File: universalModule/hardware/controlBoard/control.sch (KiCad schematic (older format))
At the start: 47 parts, among them J1 ESP_JTAG, J2 OLED_DISPLAY, Q4 BC817, Q5 BC817, SW3 SW_Push, SW4 SW_Push, SW5 SW_Push, SW6 SW_Push, SW7 SW_Push, U6 ESP32-WROVER, U7 ICM-20948, U8 CP2102N-A01-GQFN28

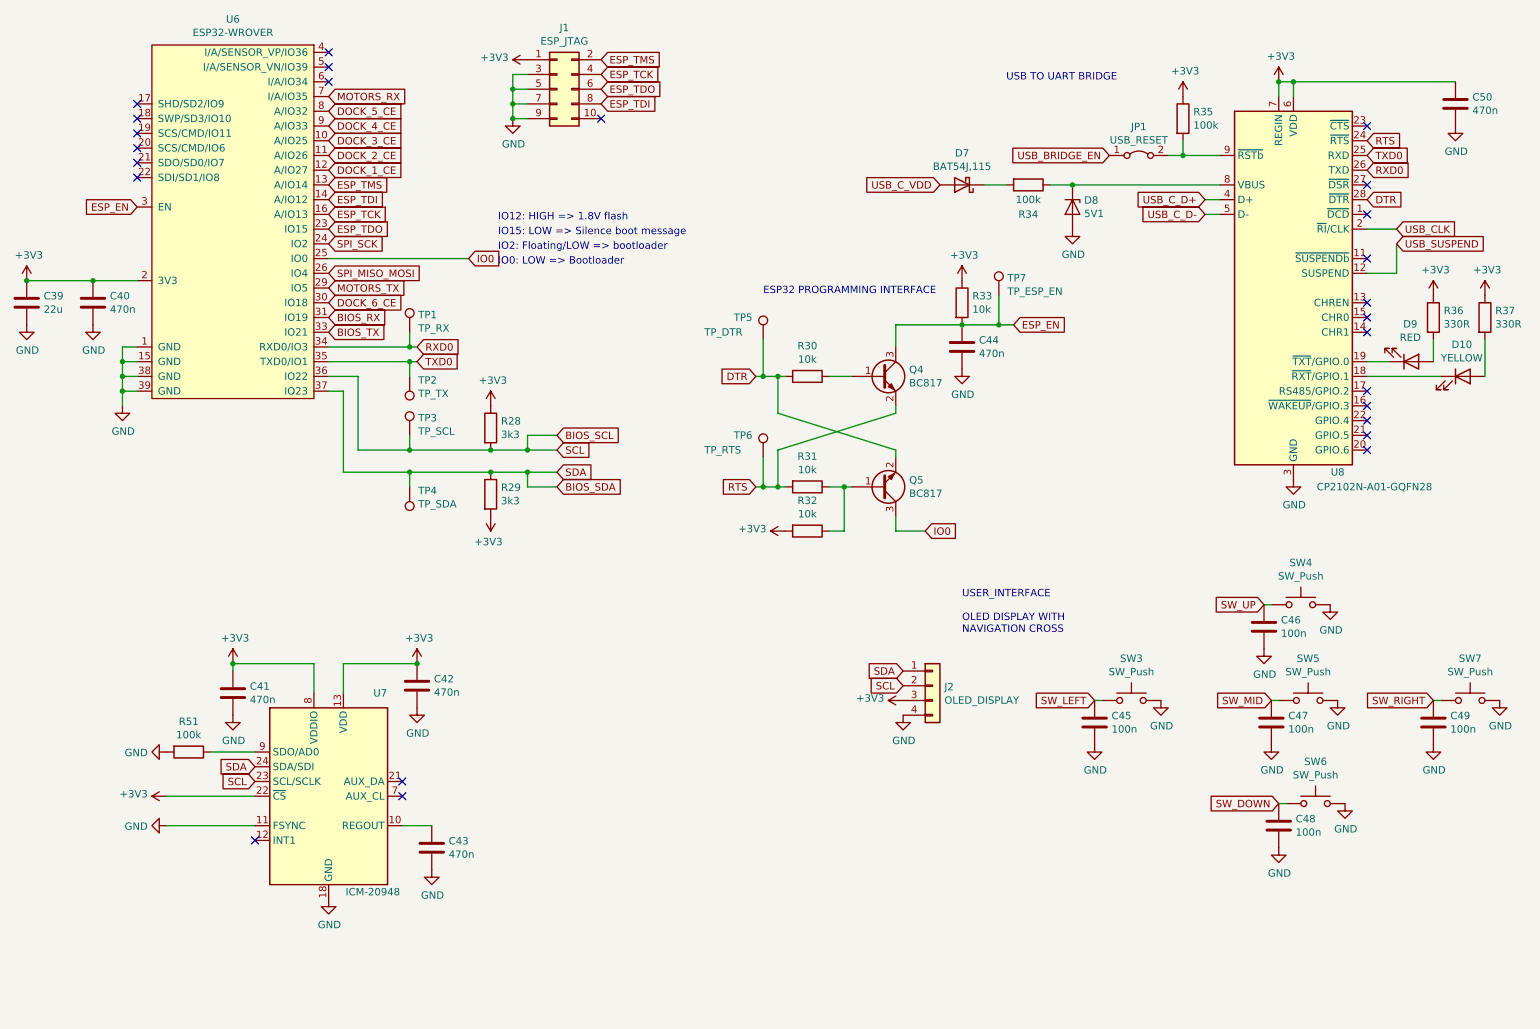
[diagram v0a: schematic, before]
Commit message: universalModule: Route the control boards
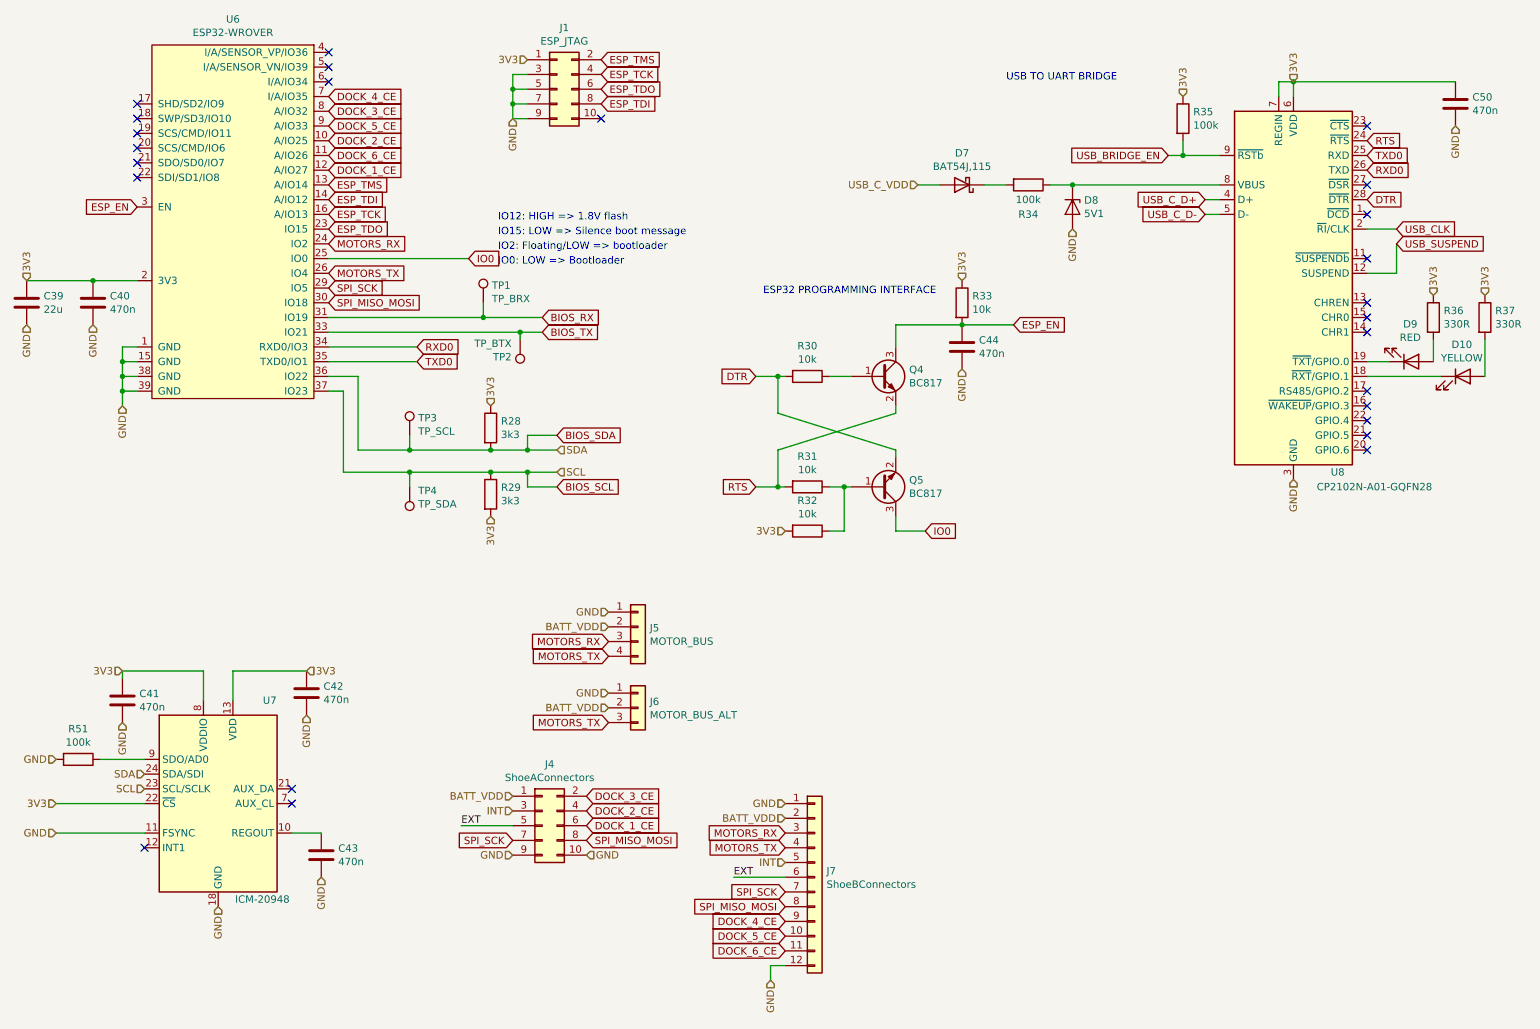
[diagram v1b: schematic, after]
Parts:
- removed C45, C46, C47, C48, C49: 100n, Capacitor_SMD:C_0402_1005Metric, symbol Device:C
- removed J2: OLED_DISPLAY, Connector_PinHeader_2.54mm:PinHeader_1x04_P2.54mm_Vertical, symbol Connector_Generic:Conn_01x04
- removed JP1: USB_RESET, Connector_PinHeader_2.00mm:PinHeader_1x01_P2.00mm_Vertical, symbol Jumper:Jumper_2_Bridged
- removed SW3, SW4, SW5, SW6, SW7: SW_Push, rofi:BUTTON_SMT_G_4_3, symbol Switch:SW_Push
- removed TP5: TP_DTR, TestPoint:TestPoint_Pad_D2.0mm, symbol Connector:TestPoint
- removed TP6: TP_RTS, TestPoint:TestPoint_Pad_D2.0mm, symbol Connector:TestPoint
- removed TP7: TP_ESP_EN, TestPoint:TestPoint_Pad_D2.0mm, symbol Connector:TestPoint
- added J4: ShoeAConnectors, Connector_PinHeader_2.00mm:PinHeader_2x05_P2.00mm_Vertical, symbol Connector_Generic:Conn_02x05_Odd_Even
- added J5: MOTOR_BUS, Connector_PinHeader_2.00mm:PinHeader_1x04_P2.00mm_Vertical, symbol Connector_Generic:Conn_01x04
- added J6: MOTOR_BUS_ALT, Connector_PinHeader_2.00mm:PinHeader_1x03_P2.00mm_Vertical, symbol Connector_Generic:Conn_01x03
- added J7: ShoeBConnectors, rofi:slipRingBrush, symbol Connector_Generic:Conn_01x12
- TP1: value TP_RX -> TP_BRX
- TP2: value TP_TX -> TP_BTX
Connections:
- net BIOS_RX: now also TP1.1
- net BIOS_SCL: now also R29.1, TP4.1, U6.37 (IO23); no longer R28.2, TP3.1, U6.36 (IO22)
- net BIOS_SDA: now also R28.2, TP3.1, U6.36 (IO22); no longer R29.1, TP4.1, U6.37 (IO23)
- net BIOS_TX: now also TP2.1
- net DOCK_1_CE: now also J4.6 (Pin_6)
- net DOCK_2_CE: now also U6.10 (A/IO25), J4.4 (Pin_4); no longer U6.11 (A/IO26)
- net DOCK_3_CE: now also U6.8 (A/IO32), J4.2 (Pin_2); no longer U6.10 (A/IO25)
- net DOCK_4_CE: now also U6.7 (I/A/IO35), J7.9 (Pin_9); no longer U6.9 (A/IO33)
- net DOCK_5_CE: now also U6.9 (A/IO33), J7.10 (Pin_10); no longer U6.8 (A/IO32)
- net DOCK_6_CE: now also U6.11 (A/IO26), J7.11 (Pin_11); no longer U6.30 (IO18)
- net GND: now also J4.10 (Pin_10), J4.9 (Pin_9), J5.1 (Pin_1), J6.1 (Pin_1), J7.1 (Pin_1), J7.12 (Pin_12)
- net MOTORS_RX: now also U6.24 (IO2), J5.3 (Pin_3), J7.3 (Pin_3); no longer U6.7 (I/A/IO35)
- net MOTORS_TX: now also U6.26 (IO4), J5.4 (Pin_4), J6.3 (Pin_3), J7.4 (Pin_4); no longer U6.29 (IO5)
- net RXD0: no longer TP1.1
- net SPI_MISO_MOSI: now also U6.30 (IO18), J4.8 (Pin_8), J7.8 (Pin_8); no longer U6.26 (IO4)
- net SPI_SCK: now also U6.29 (IO5), J4.7 (Pin_7), J7.7 (Pin_7); no longer U6.24 (IO2)
- net TXD0: no longer TP2.1
- net USB_BRIDGE_EN: now also R35.2, U8.9 (~RSTb)
- net +3V3 renamed 3V3
- new net BATT_VDD: J4.1 (Pin_1), J5.2 (Pin_2), J6.2 (Pin_2), J7.2 (Pin_2)
- new net EXT: J4.5 (Pin_5), J7.6 (Pin_6)
- new net INT: J4.3 (Pin_3), J7.5 (Pin_5)
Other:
- note removed: "USER_INTERFACE\n\nOLED DISPLAY WITH\nNAVIGATION CROSS"
- moved on the sheet: C41, C42, C43, R51, U7

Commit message: universalModule: Fine tune the control board
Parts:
- U6: #manf ESP32-WROVER-B (16MB) -> 356-ESP32-WROB(16MB)
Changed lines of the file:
@@
 F 2 "rofi:ESP32-WROVER" H 2200 2950 50  0001 C CNN
 F 3 "https://www.espressif.com/sites/default/files/documentation/esp32-wrover_datasheet_en.pdf" H 2200 2950 50  0001 C CNN
-F 4 "ESP32-WROVER-B (16MB)" H 2200 2000 50  0001 C CNN "#manf"
+F 4 "356-ESP32-WROB(16MB)" H 2200 2000 50  0001 C CNN "#manf"
 	1    2200 2000
 	1    0    0    -1

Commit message: UniversalModule: Start version 2
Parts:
- removed C44, C50: 470n, Capacitor_SMD:C_0402_1005Metric, symbol Device:C
- removed D10: YELLOW, LED_SMD:LED_0603_1608Metric, symbol Device:LED
- removed D7: BAT54J,115, Diode_SMD:D_SOD-323, symbol Device:D_Schottky
- removed D8: 5V1, Diode_SMD:D_SOD-323, symbol Device:D_Zener
- removed D9: RED, LED_SMD:LED_0603_1608Metric, symbol Device:LED
- removed Q4, Q5: BC817, Package_TO_SOT_SMD:SOT-23, symbol Transistor_BJT:BC817
- removed R30, R31, R32, R33: 10k, Resistor_SMD:R_0402_1005Metric, symbol Device:R
- removed R34, R35: 100k, Resistor_SMD:R_0402_1005Metric, symbol Device:R
- removed R36, R37: 330R, Resistor_SMD:R_0402_1005Metric, symbol Device:R
- removed TP1: TP_BRX, TestPoint:TestPoint_Pad_D2.0mm, symbol Connector:TestPoint
- removed TP2: TP_BTX, TestPoint:TestPoint_Pad_D2.0mm, symbol Connector:TestPoint
- removed U8: CP2102N-A01-GQFN28, Package_DFN_QFN:QFN-28-1EP_5x5mm_P0.5mm_EP3.35x3.35mm, symbol Interface_USB:CP2102N-A01-GQFN28
- added C?: 22u, Capacitor_SMD:C_0805_2012Metric, symbol Device:C
- added C? (x3): 470n, Capacitor_SMD:C_0402_1005Metric, symbol Device:C
- added J?: USB_ALT, Connector_PinHeader_2.54mm:PinHeader_1x04_P2.54mm_Vertical, symbol Connector_Generic:Conn_01x04
- added J?: USB_C_Receptacle_USB2.0, rofi:USB_C_Female-16Pin-HPJF, symbol Connector:USB_C_Receptacle_USB2.0
- added J?: BIOS_SWD, Connector_PinHeader_2.54mm:PinHeader_2x03_P2.54mm_Vertical, symbol Connector_Generic:Conn_01x05
- added R? (x2): 2k2, Resistor_SMD:R_0402_1005Metric, symbol Device:R
- added R? (x5): 10k, Resistor_SMD:R_0402_1005Metric, symbol Device:R
- added R? (x2): 68k, Resistor_SMD:R_0402_1005Metric, symbol Device:R
- added R?: 20k, Resistor_SMD:R_0402_1005Metric, symbol Device:R
- added TP?: TP_BAT, TestPoint:TestPoint_Pad_D2.0mm, symbol Connector:TestPoint
- added U?: STM32L432KBUx, Package_DFN_QFN:QFN-32-1EP_5x5mm_P0.5mm_EP3.45x3.45mm, symbol MCU_ST_STM32L4:STM32L432KBUx
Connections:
- net IO0 is gone; now on net BIOS_TX: U6.25 (IO0)
- net 3V3: now also C?.1, C?.1, C?.1, C?.1, J?.4 (Pin_4), U?.1 (VDD), U?.17 (VDD), U?.5 (VDDA)
- net BIOS_RX: now also U6.24 (IO2), U?.8 (PA2); no longer U6.31 (IO19)
- net BIOS_TX: now also U?.25 (PA15); no longer U6.33 (IO21)
- net GND: now also C?.2, C?.2, C?.2, C?.2, J?.1 (Pin_1), J?.5 (Pin_5), J?.A1 (GND), J?.A12 (GND), J?.B1 (GND), J?.B12 (GND), J?.S1 (SHIELD), R?.2, R?.2, R?.2, U?.16 (VSS), U?.32 (VSS), U?.33 (VSS)
- net INT: now also R?.1
- net MOTORS_RX: now also U6.33 (IO21); no longer U6.24 (IO2)
- net RXD0: now also U?.19 (PA9)
- net SPI_MISO_MOSI: now also U6.31 (IO19); no longer U6.30 (IO18)
- net SPI_SCK: now also U6.30 (IO18); no longer U6.29 (IO5)
- net TXD0: now also U?.20 (PA10)
- net USB_C_D+: now also J?.3 (Pin_3), J?.A6 (D+), J?.B6 (D+), R?.1, R?.2, U?.22 (PA12)
- net USB_C_D-: now also J?.2 (Pin_2), J?.A7 (D-), J?.B7 (D-), R?.1, R?.2, U?.21 (PA11)
- net USB_C_VDD: now also J?.4 (Pin_4), J?.A4 (VBUS), J?.A9 (VBUS), J?.B4 (VBUS), J?.B9 (VBUS), R?.1
- new net BATT_VOLTAGE: R?.1, R?.2, U?.11 (PA5)
- new net BAT_VDD: R?.1, TP?.1
- new net BUS_VOLTAGE: R?.1, R?.2, U?.9 (PA3)
- new net QC_10_N: R?.2
- new net QC_10_P: R?.2
- new net QC_2_M: R?.1
- new net QC_2_P: R?.1
- new net SWCLK: J?.1 (Pin_1), U?.24 (PA14)
- new net SWDIO: J?.2 (Pin_2), U?.23 (PA13)
- new net SWRST: J?.3 (Pin_3), U?.4 (NRST)
- new net USB_VOLTAGE: R?.1, R?.2, U?.10 (PA4)
- no-connect marks 25 -> 17
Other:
- note added: "QuickCharge 3"
- note added: "https://github.com/Crypter/QC3Client/\nhttp://blog.deconinck.info/post/2017/08/09/Turning-a-Quick-Charge-3.0-charger-into-a-variable-voltage-power-supply"
- note removed: "ESP32 PROGRAMMING INTERFACE"
- note removed: "USB TO UART BRIDGE"
- moved on the sheet: J4, J7
